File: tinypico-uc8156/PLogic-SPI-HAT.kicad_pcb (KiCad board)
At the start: 2 copper layers, 36 x 18 mm, 14 parts, among them J1 C262568, Q1 FET P-CH 60V 620Ma, Q2 MOSFET N-CH 30V 1.4A SC-70-3, U1 TinypicoESP32_Symbol

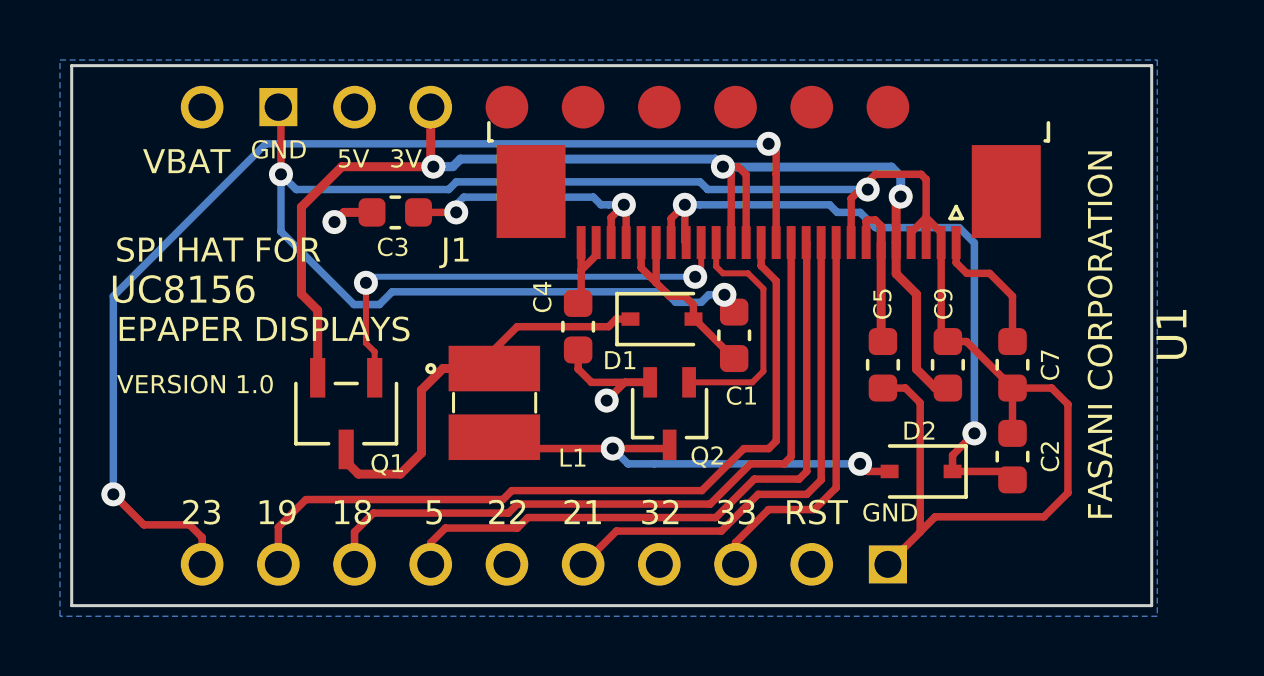
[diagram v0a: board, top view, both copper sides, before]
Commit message: Move out RST from IO21->32
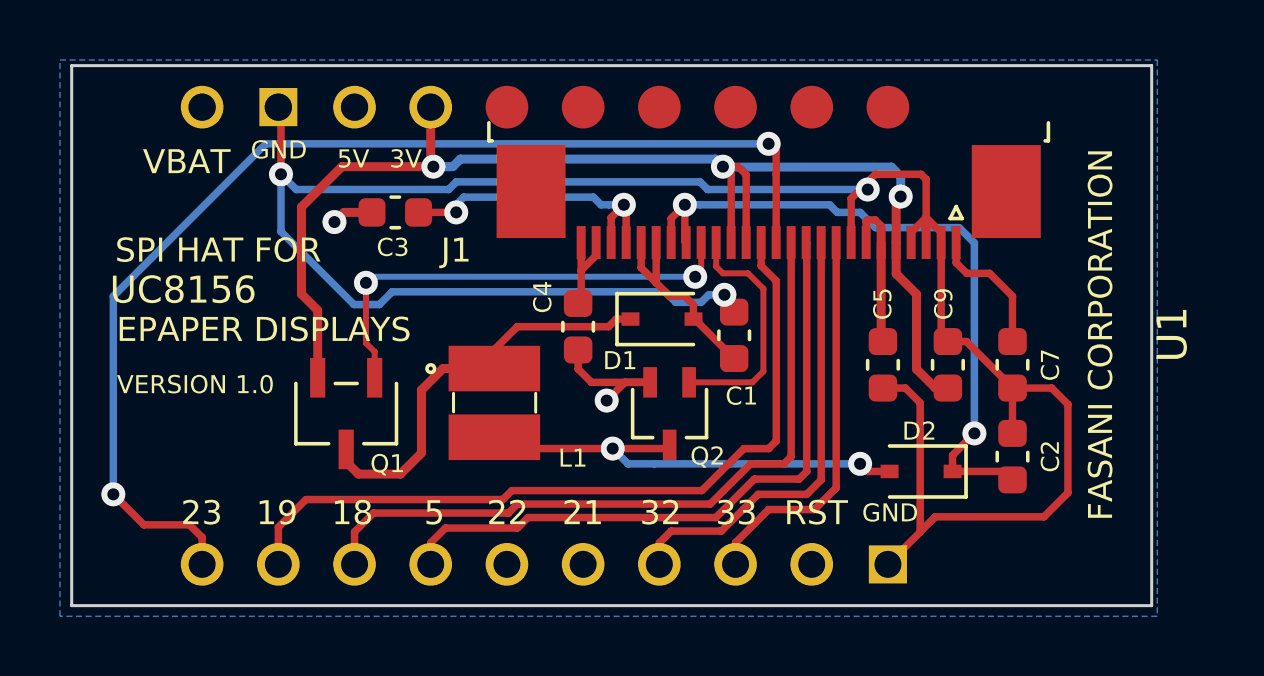
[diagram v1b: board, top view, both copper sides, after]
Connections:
- U1 pad 14: unconnected-(U1-Pad14) -> /SPI_RST_N
- U1 pad 15: /SPI_RST_N -> unconnected-(U1-Pad15)
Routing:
- net /SPI_RST_N: track 17.0 -> 14.9 mm
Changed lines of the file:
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@@
   (net 19 "unconnected-(J1-PadMP)")
   (net 20 "unconnected-(U1-Pad5)")
-  (net 21 "unconnected-(U1-Pad14)")
+  (net 21 "unconnected-(U1-Pad15)")
   (net 22 "unconnected-(U1-Pad1)")
   (net 23 "unconnected-(U1-Pad3)")
@@
       (net 10 "/VDDA") (pinfunction "11") (pintype "input"))
     (pad "17" smd rect (at 1.75 -1.35 180) (size 0.3 1.1) (layers "F.Cu" "F.Paste" "F.Mask")
-      (net 5 "/GDR_N") (pinfunction "10") (pintype "input"))
+      (net 5 "/GDR_N") (pinfunction "10") (pintype "output"))
     (pad "18" smd rect (at 2.25 -1.35 180) (size 0.3 1.1) (layers "F.Cu" "F.Paste" "F.Mask")
       (net 3 "/GDR_P") (pinfunction "9") (pintype "input"))
@@
       (net 11 "/SPI_BUSY_N") (pinfunction "IO33") (pintype "bidirectional") (solder_mask_margin 0.0254))
     (pad "14" thru_hole circle (at -7.51 1.304 90) (size 1.4224 1.4224) (drill 0.9) (layers *.Cu *.Mask)
-      (net 21 "unconnected-(U1-Pad14)") (pinfunction "IO32") (pintype "bidirectional+no_connect") (solder_mask_margin 0.0254))
+      (net 12 "/SPI_RST_N") (pinfunction "IO32") (pintype "bidirectional") (solder_mask_margin 0.0254))
     (pad "15" thru_hole circle (at -7.51 -1.236 90) (size 1.4224 1.4224) (drill 0.9) (layers *.Cu *.Mask)
-      (net 12 "/SPI_RST_N") (pinfunction "IO21") (pintype "bidirectional") (solder_mask_margin 0.0254))
+      (net 21 "unconnected-(U1-Pad15)") (pinfunction "IO21") (pintype "bidirectional+no_connect") (solder_mask_margin 0.0254))
     (pad "16" thru_hole circle (at -7.51 -3.776 90) (size 1.4224 1.4224) (drill 0.9) (layers *.Cu *.Mask)
       (net 30 "unconnected-(U1-Pad16)") (pinfunction "IO22") (pintype "bidirectional+no_connect") (solder_mask_margin 0.0254))
@@
   (footprint "PLogic:FET_SI1308EDL-SOT-323" (layer "F.Cu")
     (at 120.172 88.0846 180)
-    (property "Category" "Discrete Semiconductor Products")
+    (property "Category" "")
     (property "Component Link 1 Description" "Manufacturer URL")
     (property "Component Link 1 URL" "http://www.infineon.com/")
@@
     (property "Component Link 3 URL" "http://www.infineon.com/dgdl/SC59-Package_Overview.pdf?folderId=db3a30431936bc4b01194dc0d34440b0&fileId=db3a30431936bc4b01194dd1aa1d40cf")
     (property "DK_Datasheet_Link" "https://www.onsemi.com/pub/Collateral/FQP27P06-D.PDF")
-    (property "DK_Detail_Page" "/product-detail/en/on-semiconductor/FQP27P06/FQP27P06-ND/965349")
+    (property "DK_Detail_Page" "")
     (property "Datasheet Version" "Rev. 1.05")
     (property "Description" "MOSFET P-CH 60V 27A TO-220")
-    (property "Digi-Key_PN" "FQP27P06-ND")
-    (property "Family" "Transistors - FETs, MOSFETs - Single")
+    (property "Digi-Key_PN" "")
+    (property "Family" "")
     (property "Green" "true")
     (property "ID max" "-0.62Â A")
     (property "IDpuls max" "-2.48Â A")
-    (property "MPN" "FQP27P06")
+    (property "MPN" "")
     (property "Manufacturer" "ON Semiconductor")
     (property "Mode" "Enhancement")
@@
     (fp_circle (center -0.65 0.4191) (end -0.5738 0.4191) (layer "F.Fab") (width 0.1) (fill none))
     (pad "1" smd rect (at -0.649999 1.0414 180) (size 0.4572 1.016) (layers "F.Cu" "F.Paste" "F.Mask")
-      (net 5 "/GDR_N") (pinfunction "1") (pintype "unspecified"))
+      (net 5 "/GDR_N") (pinfunction "1") (pintype "input"))
     (pad "2" smd rect (at 0.649999 1.0414 180) (size 0.4572 1.016) (layers "F.Cu" "F.Paste" "F.Mask")
-      (net 6 "GND") (pinfunction "2") (pintype "unspecified"))
+      (net 6 "GND") (pinfunction "2") (pintype "power_in"))
     (pad "3" smd rect (at 0 -1.0414 180) (size 0.4572 1.016) (layers "F.Cu" "F.Paste" "F.Mask")
-      (net 2 "Net-(D2-Pad2)") (pinfunction "3") (pintype "unspecified"))
+      (net 2 "Net-(D2-Pad2)") (pinfunction "3") (pintype "output"))
     (model "${KIPRJMOD}/parts/3d/MOSFET_8EDL-T1-GE3_VIS.step"
       (offset (xyz 0 0 0))
@@
   (segment (start 125.224 90.296) (end 124.744 90.776) (width 0.25) (layer "F.Cu") (net 12))
   (segment (start 123.124 90.776) (end 121.9 92) (width 0.25) (layer "F.Cu") (net 12))
-  (segment (start 118.4 92) (end 117.29 93.11) (width 0.25) (layer "F.Cu") (net 12))
-  (segment (start 121.9 92) (end 118.4 92) (width 0.25) (layer "F.Cu") (net 12))
+  (segment (start 121.9 92) (end 120.225 92) (width 0.25) (layer "F.Cu") (net 12))
+  (segment (start 119.83 92.395) (end 119.83 93.11) (width 0.25) (layer "F.Cu") (net 12))
+  (segment (start 120.225 92) (end 119.83 92.395) (width 0.25) (layer "F.Cu") (net 12))
   (segment (start 112.7 91.9) (end 112.21 92.39) (width 0.25) (layer "F.Cu") (net 13))
   (segment (start 124.744 82.403) (end 124.744 90.014) (width 0.25) (layer "F.Cu") (net 13))
